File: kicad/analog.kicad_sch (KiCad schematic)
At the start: 17 parts, among them U1 MP2672GD-0000-Z, U3 MP2236CGJ-Z, U301 MR30-Vertical, U302 MP2236CGJ-Z

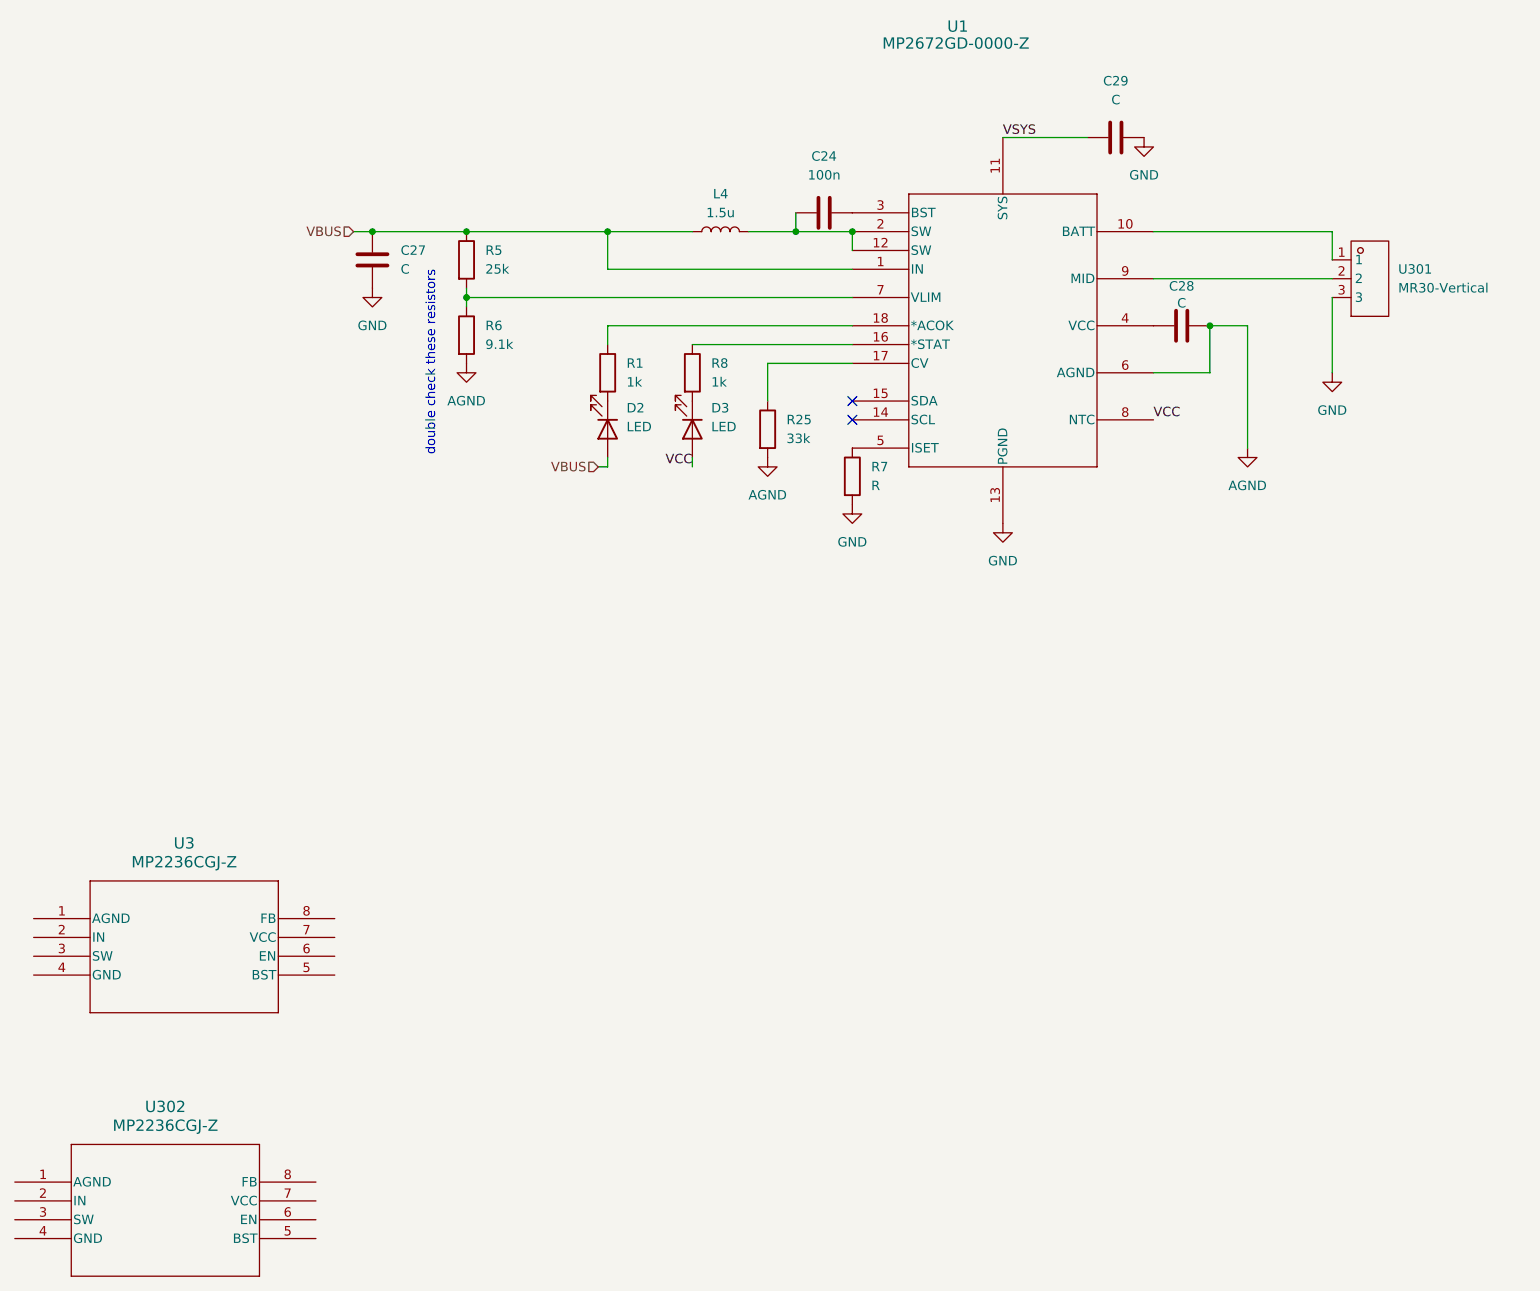
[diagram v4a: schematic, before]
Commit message: delete old buck, replace with buck/boost
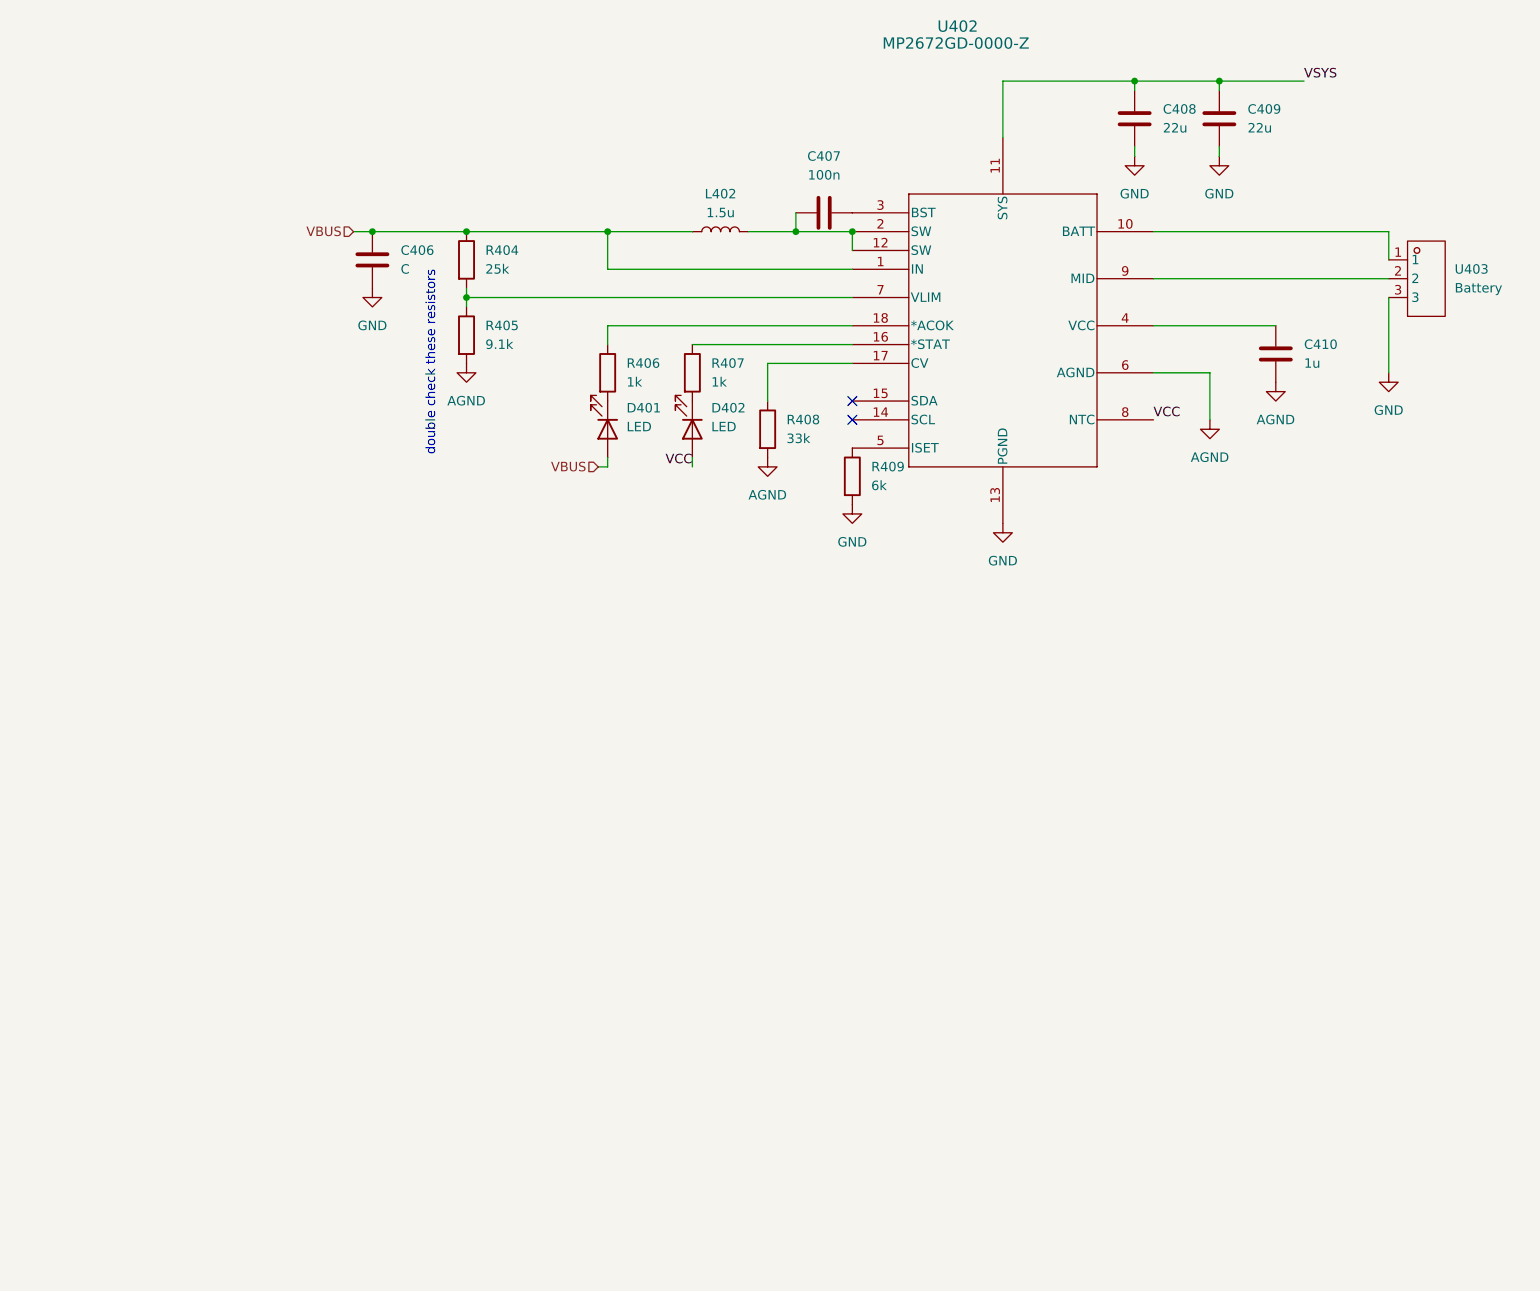
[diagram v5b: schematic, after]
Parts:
- removed C28: C, symbol Device:C
- removed U3, U302: MP2236CGJ-Z, 4in-power:TSOT23-8_MP2236C_MNP, symbol 4in-power:MP2236CGJ-Z
- added C409: 22u, symbol Device:C
- added C410: 1u, symbol Device:C
- C408: renamed from C29; value C -> 22u
- R409: renamed from R7; value R -> 6k
- U403: renamed from U301; value MR30-Vertical -> Battery
- renumbered C27 to C406, C24 to C407, D2 to D401, D3 to D402, L4 to L402, R5 to R404, R6 to R405, R1 to R406, R8 to R407, R25 to R408, U1 to U402
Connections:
- net AGND: now also C410.1
- net GND: now also C408.1, C409.1; no longer C408.2
- net VSYS: now also C408.2, C409.2; no longer C408.1
- net at U402.4 (VCC): now also C410.2
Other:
- moved on the sheet: C408, U403

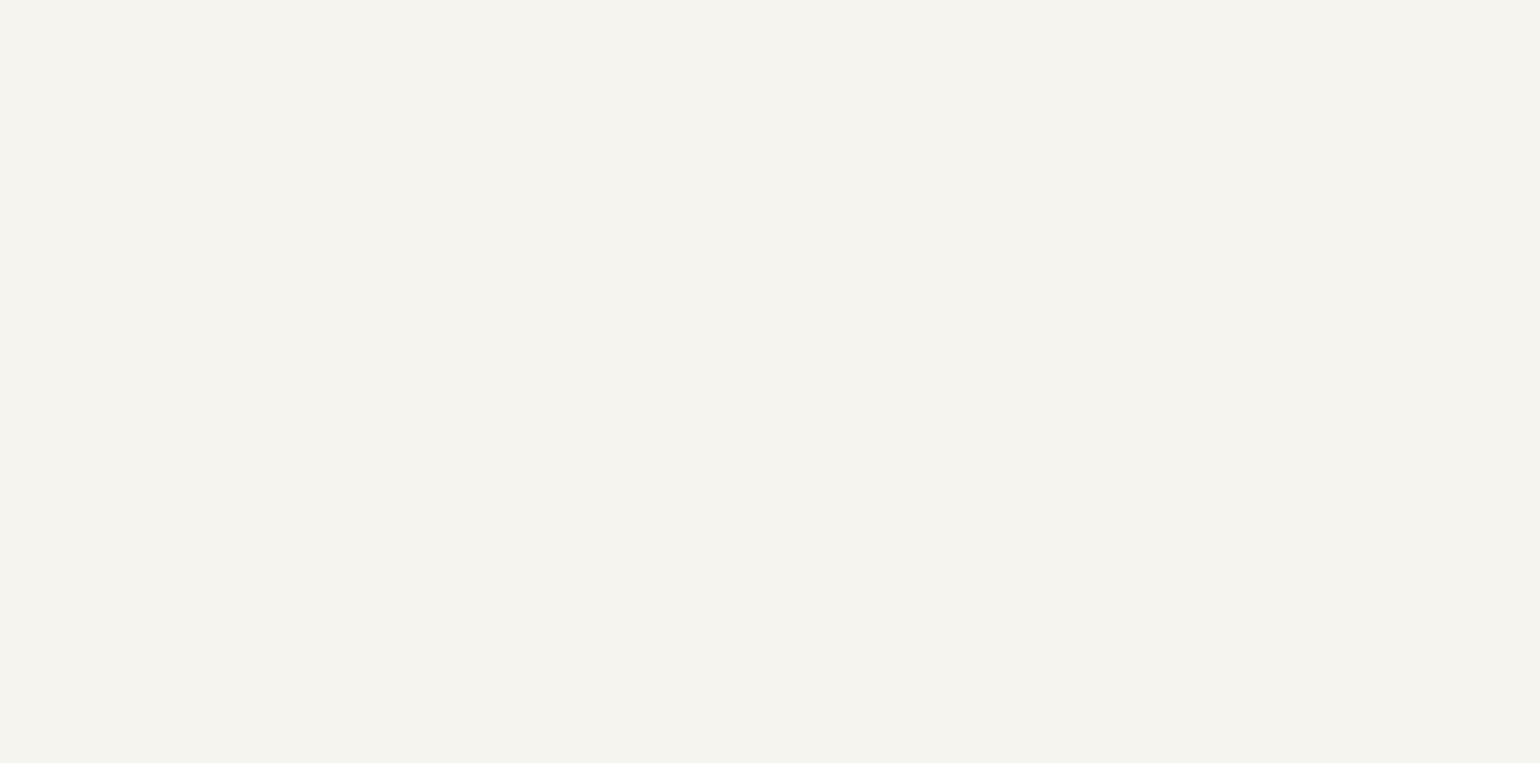
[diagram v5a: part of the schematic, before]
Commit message: add 5v buck-boost schematic
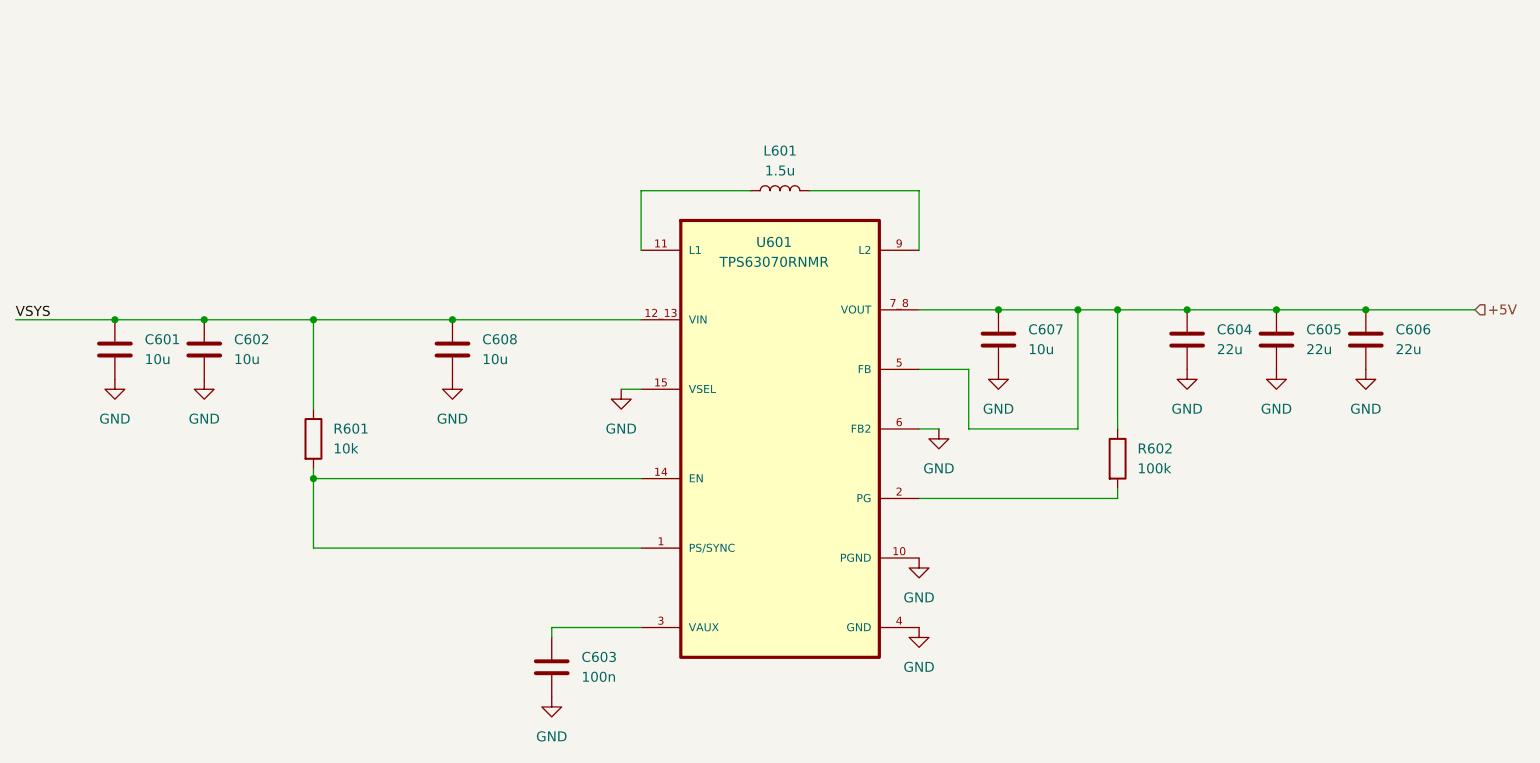
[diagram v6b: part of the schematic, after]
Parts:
- added C601, C602, C607, C608: 10u, symbol Device:C
- added C603: 100n, symbol Device:C
- added C604, C605, C606: 22u, symbol Device:C
- added L601: 1.5u, symbol Device:L
- added R601: 10k, symbol Device:R
- added R602: 100k, symbol Device:R
- added U601: TPS63070RNMR, 4in-power:VREG_TPS63070RNMR, symbol 4in-power:TPS63070RNMR
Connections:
- net GND: now also C601.2, C602.2, C603.2, C604.2, C605.2, C606.2, C607.2, C608.2, U601.10 (PGND), U601.15 (VSEL), U601.4 (GND), U601.6 (FB2)
- net VSYS: now also C601.1, C602.1, C608.1, R601.1, U601.12_13 (VIN)
- new net: R601.2, U601.1 (PS/SYNC), U601.14 (EN)
- new net: L601.1, U601.11 (L1)
- new net: R602.2, U601.2 (PG)
- new net: C603.1, U601.3 (VAUX)
- new net: L601.2, U601.9 (L2)
- new net +5V: C604.1, C605.1, C606.1, C607.1, R602.1, U601.5 (FB), U601.7_8 (VOUT)

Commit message: complete 5v and 3v buck-boost schematic
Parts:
- added C201, C202, C203, C205: 10u, symbol Device:C
- added C204: 100n, symbol Device:C
- added C206, C207, C208: 22u, symbol Device:C
- added L201: 1.5u, symbol Device:L
- added R203: 10k, symbol Device:R
- added R204: 100k, symbol Device:R
- added R205: 470k, symbol Device:R
- added R206: 150k, symbol Device:R
- added U202: TPS63070RNMR, 4in-power:VREG_TPS63070RNMR, symbol 4in-power:TPS63070RNMR
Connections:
- net GND: now also C201.2, C202.2, C203.2, C204.2, C205.2, C206.2, C207.2, C208.2, R206.2, U202.10 (PGND), U202.15 (VSEL), U202.4 (GND), U202.6 (FB2)
- net VSYS: now also C201.1, C202.1, C203.1, R203.1, U202.12_13 (VIN)
- new net: R203.2, U202.1 (PS/SYNC), U202.14 (EN)
- new net: R205.2, R206.1, U202.5 (FB)
- new net: R204.2, U202.2 (PG)
- new net: C204.1, U202.3 (VAUX)
- new net: L201.1, U202.11 (L1)
- new net: L201.2, U202.9 (L2)
- new net +3.3V: C205.1, C206.1, C207.1, C208.1, R204.1, R205.1, U202.7_8 (VOUT)
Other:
- note added: "3.3V Buck-boost"
- note added: "5V Buck-boost"
- note added: "Charging, balancing, switching IC"
- moved on the sheet: C406, C407, C408, C409, C410, C601, C602, C603, C604, C605, C606, C607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

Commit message: add LCSC PNs and footprints for various components, import custom step file for inductor
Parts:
- C406: value C -> 10u
- C407, C603: footprint (none) -> Capacitor_SMD:C_0402_1005Metric; JLC Link (none) -> https://jlcpcb.com/partdetail/291005-CL05B104KB54PNC/C307331; LCSC PN (none) -> C307331
- C410: footprint (none) -> Capacitor_SMD:C_0402_1005Metric; JLC Link (none) -> https://jlcpcb.com/partdetail/53938-CL05A105KA5NQNC/C52923; LCSC PN (none) -> C52923
- C504: renamed from C204; footprint (none) -> Capacitor_SMD:C_0402_1005Metric; JLC Link (none) -> https://jlcpcb.com/partdetail/291005-CL05B104KB54PNC/C307331; LCSC PN (none) -> C307331
- L402, L601: footprint (none) -> 4in-power:IND-SMD_L4.0-W4.0_YSMC0420V; JLC Link (none) -> https://jlcpcb.com/partdetail/YJYCOIN-YSMC0420V1R5M/C196307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; LCSC PN (none) -> C19630740
- L501: renamed from L201; footprint (none) -> 4in-power:IND-SMD_L4.0-W4.0_YSMC0420V; JLC Link (none) -> https://jlcpcb.com/partdetail/YJYCOIN-YSMC0420V1R5M/C196307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; LCSC PN (none) -> C19630740
- R406, R407: footprint (none) -> Resistor_SMD:R_0402_1005Metric; JLC Link (none) -> https://jlcpcb.com/partdetail/12256-0402WGF1001TCE/C11702; LCSC PN (none) -> C11702
- R409: JLC Link (none) -> https://jlcpcb.com/partdetail/VikingTech-ARG05BTC6001N/C282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; LCSC PN (none) -> C2828725
- R501: renamed from R203; footprint (none) -> Resistor_SMD:R_0402_1005Metric; JLC Link (none) -> https://jlcpcb.com/partdetail/26487-0402WGF1002TCE/C25744; LCSC PN (none) -> C25744
- R601: footprint (none) -> Resistor_SMD:R_0402_1005Metric; JLC Link (none) -> https://jlcpcb.com/partdetail/26487-0402WGF1002TCE/C25744; LCSC PN (none) -> C25744
- U402: DigKey Link (none) -> https://www.digikey.ca/en/products/detail/monolithic-power-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; JLC Link (none) -> https://jlcpcb.com/partdetail/3007016-MP2672GD_0000Z/C28372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; Manufacturer PN (none) -> MP2672GD-0000-P
- renumbered C201 to C501, C202 to C502, C203 to C503, C205 to C505, C206 to C506, C207 to C507, C208 to C508, R205 to R502, R206 to R503, R204 to R504, U202 to U501
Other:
- moved on the sheet: C406
